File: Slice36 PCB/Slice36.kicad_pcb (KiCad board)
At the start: 2 copper layers, 118.8 x 97.2 mm, 52 parts, among them J1 AudioJack4, J2 AudioJack4, Sw1 Cherry_Doublesided, Sw10 Cherry_Doublesided, Sw11 Cherry_Doublesided, Sw12 Cherry_Doublesided, Sw13 Cherry_Doublesided, Sw14 Cherry_Doublesided, Sw15 Cherry_Doublesided, Sw16 Cherry_Doublesided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

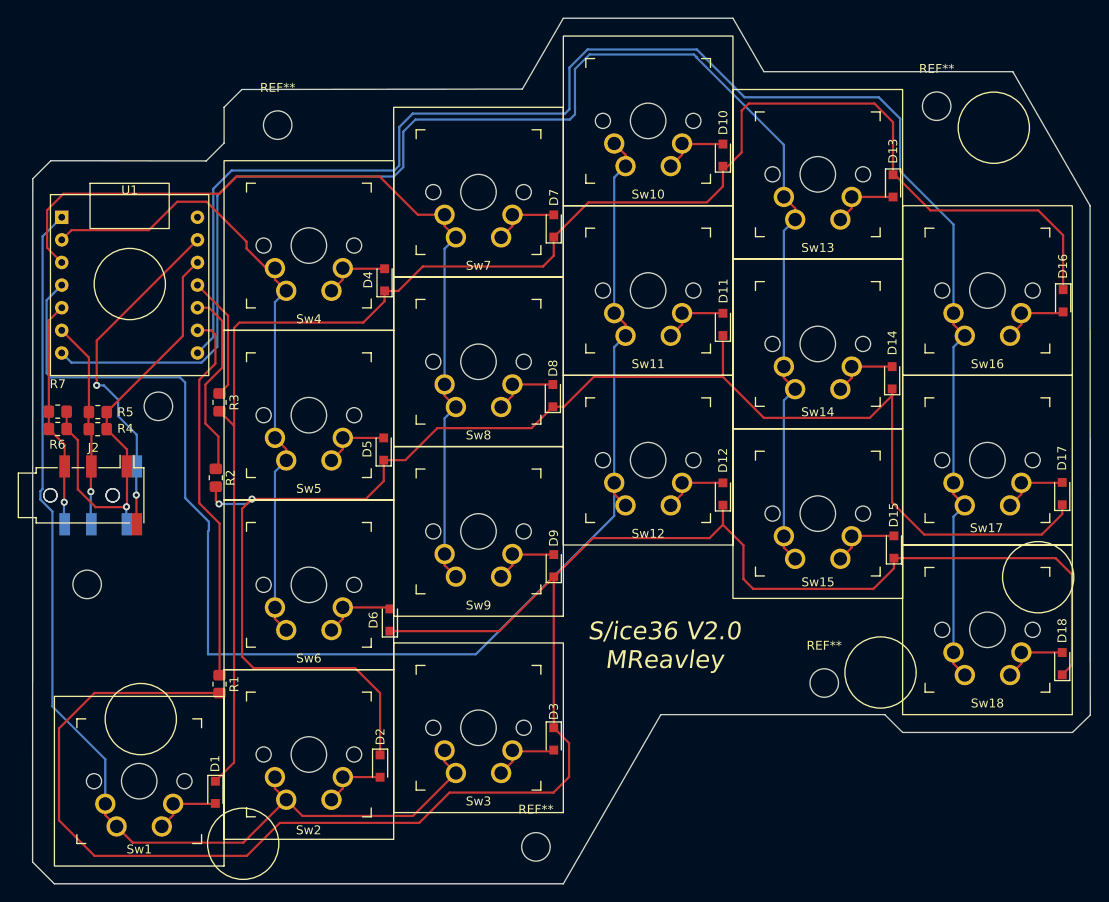
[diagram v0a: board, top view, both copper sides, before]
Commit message: Convert switchs to Kailh Choc V1, update routes
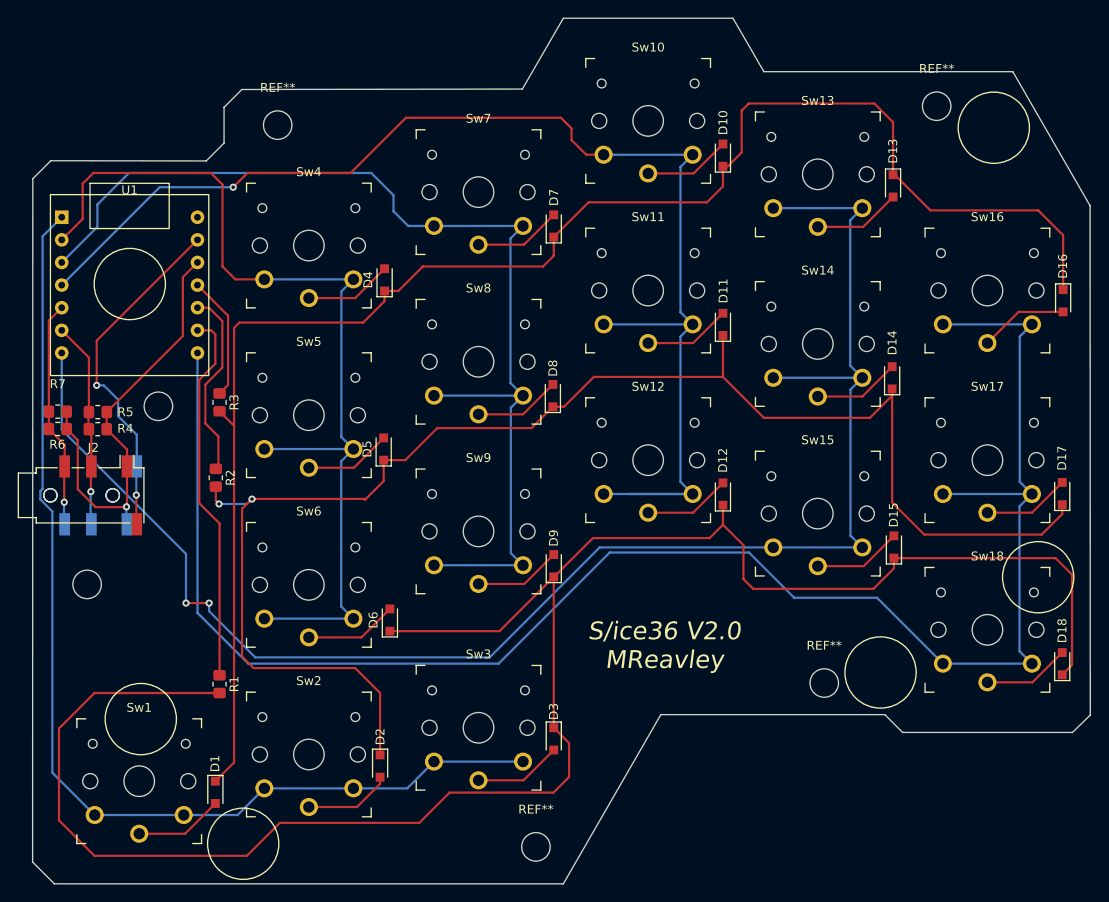
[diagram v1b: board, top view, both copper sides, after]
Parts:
- Sw1, Sw10, Sw11, Sw12, Sw13, Sw14, Sw15, Sw16, Sw17, Sw18, Sw2, Sw3, Sw4, Sw5, Sw6, Sw7, Sw8, Sw9: value Cherry_Doublesided -> choc_v1_dbl; footprint MxSwitches:SW_MX_reversible -> Slice36 PCB:SW_PG1350_reversible
- turned Sw1 to 0 degrees
- turned Sw10 to 0 degrees
- turned Sw11 to 0 degrees
- turned Sw12 to 0 degrees
- turned Sw13 to 0 degrees
- turned Sw14 to 0 degrees
- turned Sw15 to 0 degrees
- turned Sw16 to 0 degrees
- turned Sw17 to 0 degrees
- turned Sw18 to 0 degrees
- turned Sw2 to 0 degrees
- turned Sw3 to 0 degrees
- turned Sw4 to 0 degrees
- turned Sw5 to 0 degrees
- turned Sw6 to 0 degrees
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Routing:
- net Net-(Sw4-Pad2): track 72.5 -> 108.9 mm
- net Net-(Sw7-Pad2): track 97.8 -> 121.3 mm
- net Net-(Sw17-Pad2): track 178.9 -> 196.0 mm
- net Net-(Sw15-Pad2): track 164.5 -> 178.3 mm, vias 0 -> 2
- net Net-(Sw10-Pad2): track 157.3 -> 148.6 mm, vias 0 -> 1
- net Net-(D2-Pad2): track 7.26 -> 9.83 mm
- net Net-(D1-Pad2): track 7.41 -> 9.96 mm
- net Net-(Sw15-Pad1): track 7.82 -> 9.96 mm
- net Net-(D17-Pad2): track 7.67 -> 9.81 mm
- net Net-(D12-Pad2): track 7.66 -> 9.79 mm
- net Net-(D14-Pad2): track 7.61 -> 9.74 mm
- net Net-(D11-Pad2): track 7.66 -> 9.79 mm
- net Net-(D5-Pad2): track 7.66 -> 9.79 mm
- net Net-(D8-Pad2): track 7.61 -> 9.74 mm
- net Net-(D7-Pad2): track 7.71 -> 9.84 mm
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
